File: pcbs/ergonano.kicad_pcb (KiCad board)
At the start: 2 copper layers, 167.6 x 164.6 mm, 92 parts

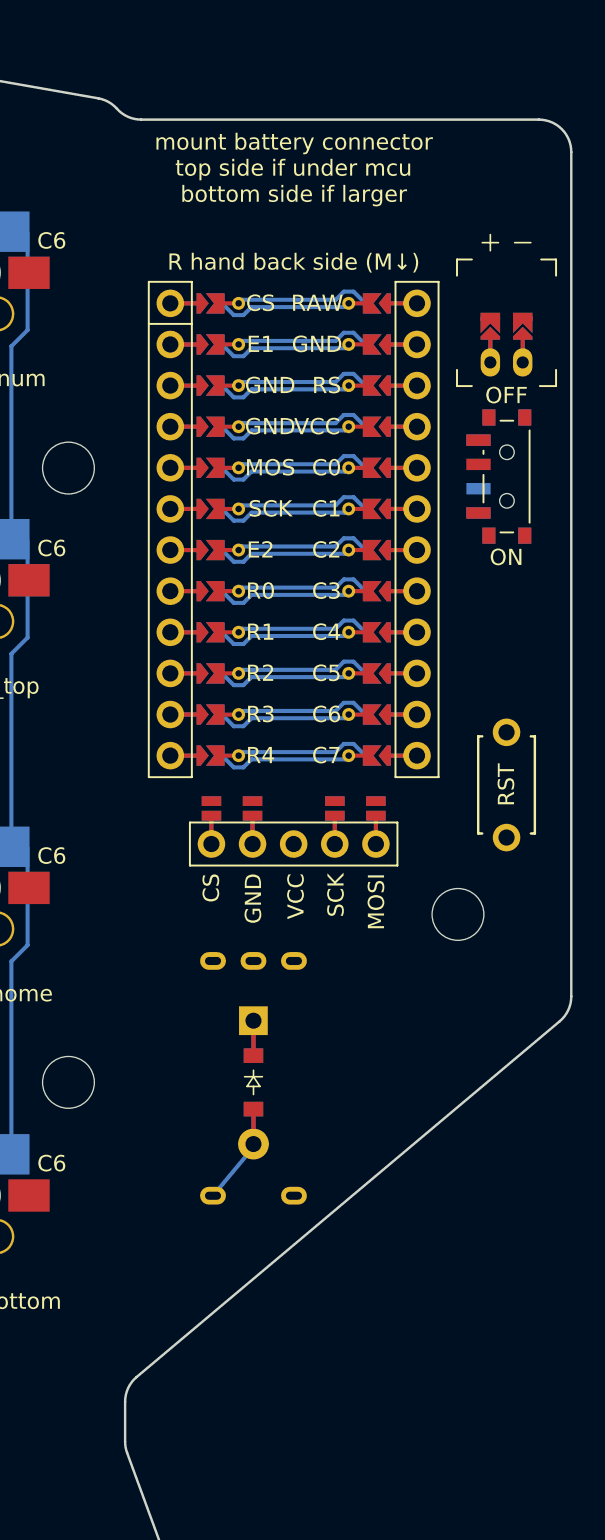
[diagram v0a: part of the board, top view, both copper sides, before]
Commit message: fully define display location with points and show on preview. Rotate encoder footprint
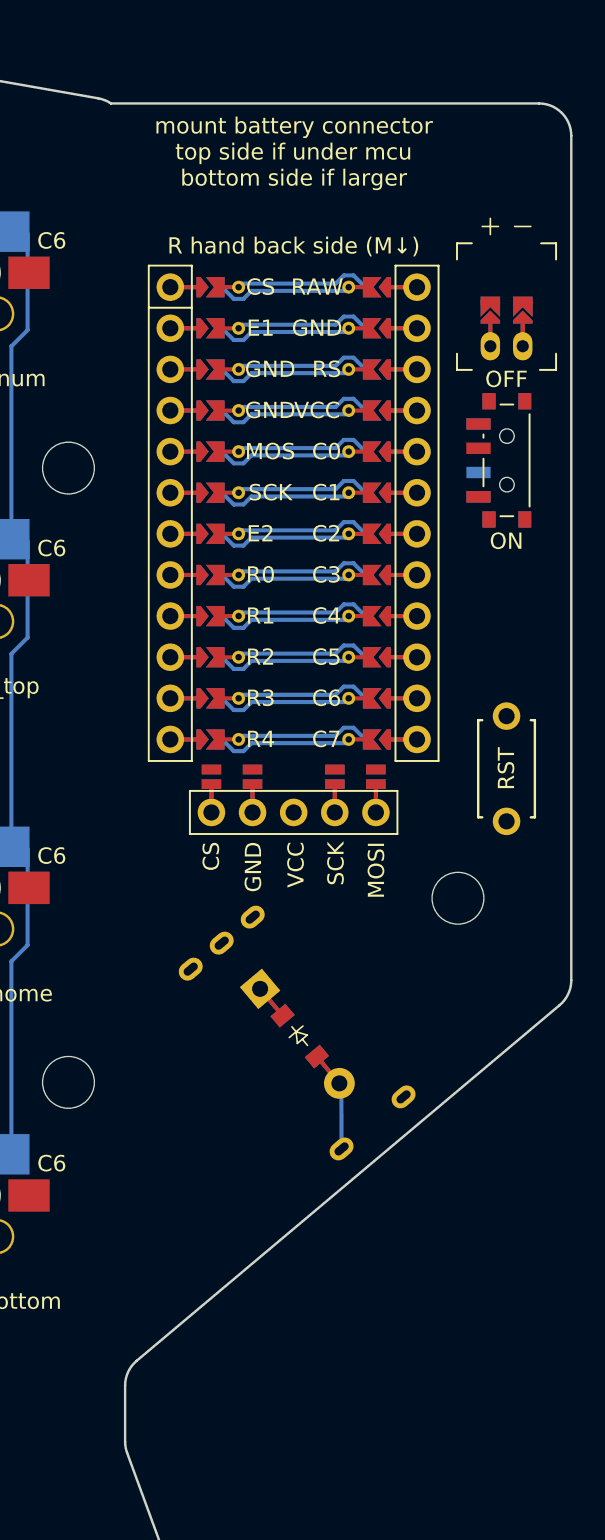
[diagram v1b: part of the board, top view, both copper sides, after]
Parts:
- moved D39 4.04 mm to (187.8, 93.6), turned to 310 degrees
- moved RE1 4.04 mm to (187.8, 93.6), turned to 220 degrees
- moved DISP1 1.95 mm to (187.4, 63.1)
- moved JST1 1.00 mm to (200.6, 51.0)
- moved MCU1 1.00 mm to (187.4, 60.0)
- moved MH9 1.00 mm to (197.6, 85.1)
- moved PWR1 1.00 mm to (200.6, 58.0)
- moved RST1 1.00 mm to (200.6, 77.1)
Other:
- outline, holes or cut-outs redrawn
